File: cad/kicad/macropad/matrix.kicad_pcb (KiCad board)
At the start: 2 copper layers, 185.5 x 88.9 mm, 54 parts, among them J1 Conn_01x27, J2 Conn_01x27, J3 Conn_01x18, U1 74HC154, U2 MCP4821, U5 CMP04, U6 CMP04

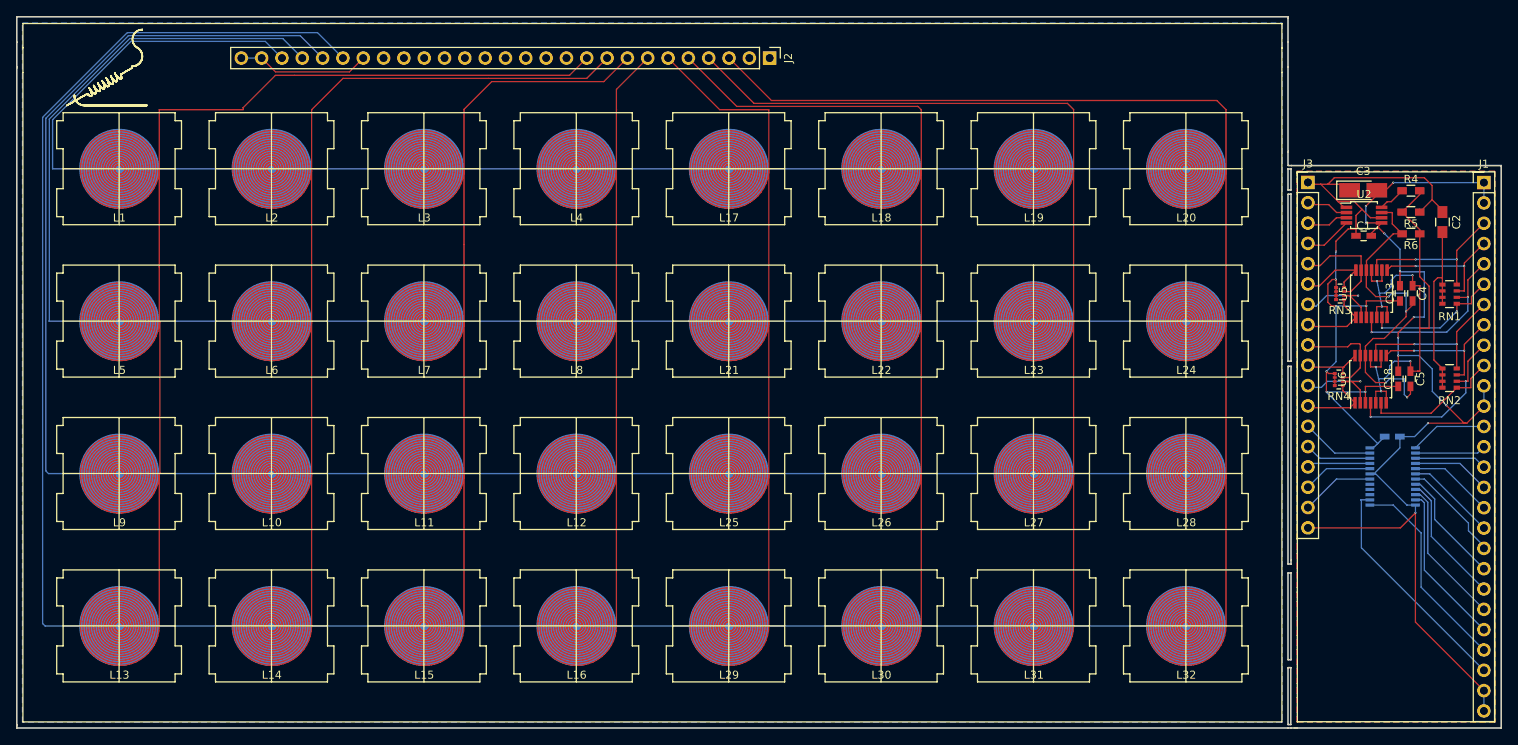
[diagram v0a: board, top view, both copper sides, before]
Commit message: seperated the controller from the demo macropad, remade the controller to hopefully be less succeptable to emi, and digital interferance.
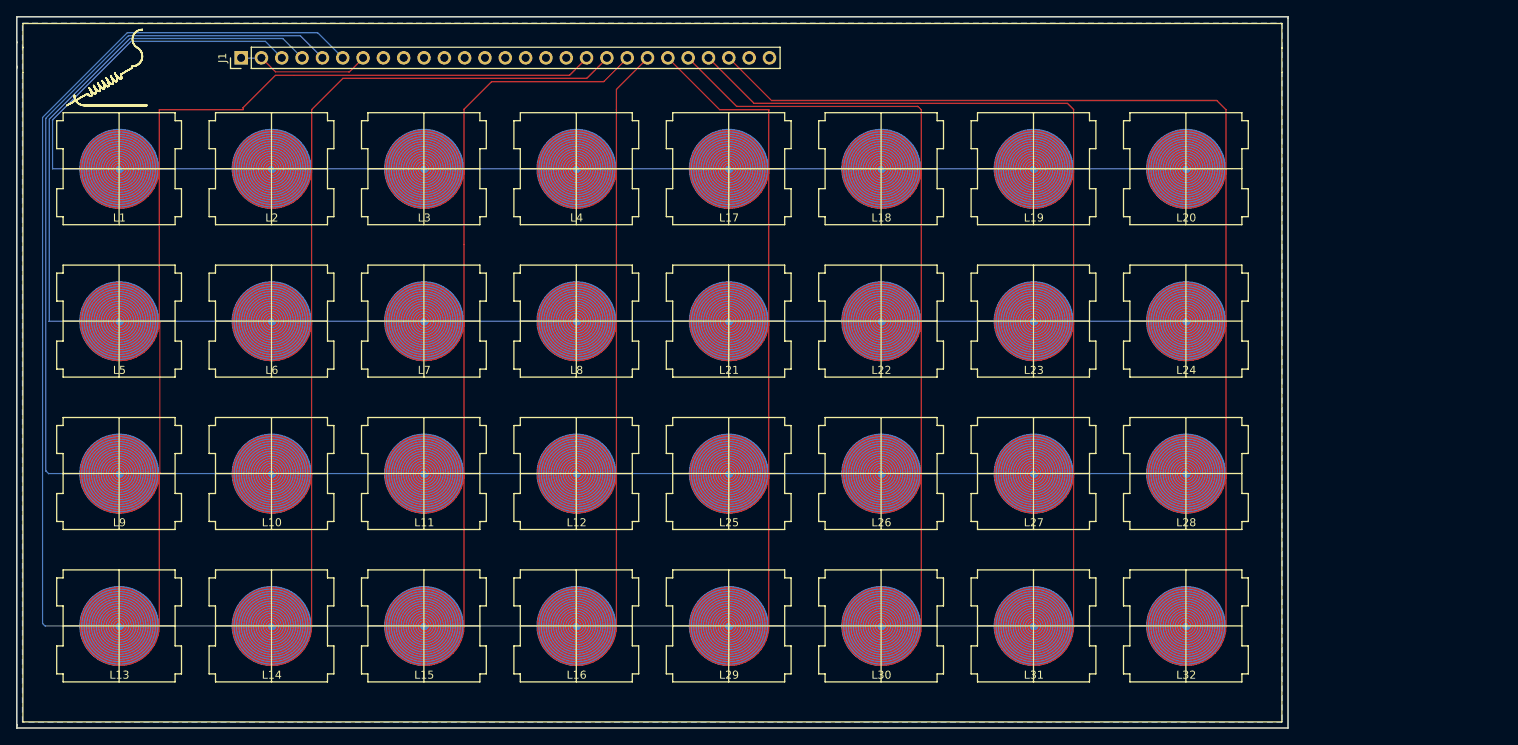
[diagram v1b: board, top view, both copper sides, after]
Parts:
- removed C1, C13, C18: 0u1, Capacitors_SMD:C_0603_HandSoldering
- removed C2: 100u, Capacitors_SMD:C_0805_HandSoldering
- removed C3: 10u-T, Capacitors_Tantalum_SMD:CP_Tantalum_Case-R_EIA-2012-12_Hand
- removed C4, C5, C9: 1u, Capacitors_SMD:C_0603_HandSoldering
- removed J2: Conn_01x27, Pin_Headers:Pin_Header_Straight_1x27_Pitch2.54mm
- removed J3: Conn_01x18, Pin_Headers:Pin_Header_Straight_1x18_Pitch2.54mm
- removed R4, R5: 20k, Resistors_SMD:R_0603_HandSoldering
- removed R6: 4k7, Resistors_SMD:R_0603_HandSoldering
- removed RN1, RN2: 330, Resistors_SMD:R_Array_Convex_4x0603
- removed RN3, RN4: 66k, Resistors_SMD:R_Array_Convex_4x0402
- removed U1: 74HC154, Housings_SSOP:TSSOP-24_4.4x7.8mm_Pitch0.65mm
- removed U2: MCP4821, Housings_SSOP:MSOP-8_3x3mm_Pitch0.65mm
- removed U5, U6: CMP04, Housings_SSOP:TSSOP-14_4.4x5mm_Pitch0.65mm
- moved J1 156.1 mm to (78.2, 48.3), turned to 90 degrees
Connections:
- J1 pad 1: GND -> GNDREF
- J1 pad 10: M8 -> GNDREF
- J1 pad 11: GND -> GNDREF
- J1 pad 12: GND -> GNDREF
- J1 pad 13: CS1 -> GNDREF
- J1 pad 14: CS2 -> GNDREF
- J1 pad 15: CS3 -> GNDREF
- J1 pad 16: CS4 -> GNDREF
- J1 pad 17: CS5 -> GNDREF
- J1 pad 18: CS6 -> /MRP1
- J1 pad 19: CS7 -> /MRP2
- J1 pad 2: GND -> GNDREF
- J1 pad 20: CS8 -> /MRP3
- J1 pad 21: CS9 -> /MRP4
- J1 pad 22: CS10 -> /MRP5
- J1 pad 23: CS11 -> /MRP6
- J1 pad 24: CS12 -> /MRP7
- J1 pad 25: CS13 -> /MRP8
- J1 pad 26: GND -> GNDREF
- J1 pad 27: GND -> GNDREF
- J1 pad 3: M1 -> /MCN13
- J1 pad 4: M2 -> /MCN12
- J1 pad 5: M3 -> /MCN11
- J1 pad 6: M4 -> /MCN10
- J1 pad 7: M5 -> GNDREF
- J1 pad 8: M6 -> GNDREF
- J1 pad 9: M7 -> GNDREF
- L1 pad 1: /matrix/MRP1 -> /MRP1
- L1 pad 2: /matrix/MCN13 -> /MCN13
- L10 pad 1: /matrix/MRP2 -> /MRP2
- L10 pad 2: /matrix/MCN11 -> /MCN11
- L11 pad 1: /matrix/MRP3 -> /MRP3
- L11 pad 2: /matrix/MCN11 -> /MCN11
- L12 pad 1: /matrix/MRP4 -> /MRP4
- L12 pad 2: /matrix/MCN11 -> /MCN11
- L13 pad 1: /matrix/MRP1 -> /MRP1
- L13 pad 2: /matrix/MCN10 -> /MCN10
- L14 pad 1: /matrix/MRP2 -> /MRP2
- L14 pad 2: /matrix/MCN10 -> /MCN10
- L15 pad 1: /matrix/MRP3 -> /MRP3
- L15 pad 2: /matrix/MCN10 -> /MCN10
- L16 pad 1: /matrix/MRP4 -> /MRP4
- L16 pad 2: /matrix/MCN10 -> /MCN10
- L17 pad 1: /matrix/MRP5 -> /MRP5
- L17 pad 2: /matrix/MCN13 -> /MCN13
- L18 pad 1: /matrix/MRP6 -> /MRP6
- L18 pad 2: /matrix/MCN13 -> /MCN13
- L19 pad 1: /matrix/MRP7 -> /MRP7
- L19 pad 2: /matrix/MCN13 -> /MCN13
- L2 pad 1: /matrix/MRP2 -> /MRP2
- L2 pad 2: /matrix/MCN13 -> /MCN13
- L20 pad 1: /matrix/MRP8 -> /MRP8
- L20 pad 2: /matrix/MCN13 -> /MCN13
- L21 pad 1: /matrix/MRP5 -> /MRP5
- L21 pad 2: /matrix/MCN12 -> /MCN12
- L22 pad 1: /matrix/MRP6 -> /MRP6
- L22 pad 2: /matrix/MCN12 -> /MCN12
- L23 pad 1: /matrix/MRP7 -> /MRP7
- L23 pad 2: /matrix/MCN12 -> /MCN12
- L24 pad 1: /matrix/MRP8 -> /MRP8
- L24 pad 2: /matrix/MCN12 -> /MCN12
- L25 pad 1: /matrix/MRP5 -> /MRP5
- L25 pad 2: /matrix/MCN11 -> /MCN11
- L26 pad 1: /matrix/MRP6 -> /MRP6
- L26 pad 2: /matrix/MCN11 -> /MCN11
- L27 pad 1: /matrix/MRP7 -> /MRP7
- L27 pad 2: /matrix/MCN11 -> /MCN11
- L28 pad 1: /matrix/MRP8 -> /MRP8
- L28 pad 2: /matrix/MCN11 -> /MCN11
- L29 pad 1: /matrix/MRP5 -> /MRP5
- L29 pad 2: /matrix/MCN10 -> /MCN10
- L3 pad 1: /matrix/MRP3 -> /MRP3
- L3 pad 2: /matrix/MCN13 -> /MCN13
- L30 pad 1: /matrix/MRP6 -> /MRP6
- L30 pad 2: /matrix/MCN10 -> /MCN10
- L31 pad 1: /matrix/MRP7 -> /MRP7
- L31 pad 2: /matrix/MCN10 -> /MCN10
- L32 pad 1: /matrix/MRP8 -> /MRP8
- L32 pad 2: /matrix/MCN10 -> /MCN10
- L4 pad 1: /matrix/MRP4 -> /MRP4
- L4 pad 2: /matrix/MCN13 -> /MCN13
- L5 pad 1: /matrix/MRP1 -> /MRP1
- L5 pad 2: /matrix/MCN12 -> /MCN12
- L6 pad 1: /matrix/MRP2 -> /MRP2
- L6 pad 2: /matrix/MCN12 -> /MCN12
- L7 pad 1: /matrix/MRP3 -> /MRP3
- L7 pad 2: /matrix/MCN12 -> /MCN12
- L8 pad 1: /matrix/MRP4 -> /MRP4
- L8 pad 2: /matrix/MCN12 -> /MCN12
- L9 pad 1: /matrix/MRP1 -> /MRP1
- L9 pad 2: /matrix/MCN11 -> /MCN11
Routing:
- net /matrix/MCN10: track 249.7 -> 0.00 mm
- net /MCN10: track 0.00 -> 249.7 mm
- net /matrix/MCN11: track 229.4 -> 0.00 mm
- net /MCN11: track 0.00 -> 229.4 mm
- net /matrix/MCN12: track 208.8 -> 0.00 mm
- net /MCN12: track 0.00 -> 208.8 mm
- net /matrix/MCN13: track 181.4 -> 0.00 mm
- net /MCN13: track 0.00 -> 181.4 mm
- net GND: track 181.1 -> 0.00 mm, vias 15 -> 0
- net /matrix/MRP8: track 129.3 -> 0.00 mm
- net /MRP8: track 0.00 -> 129.3 mm
- net /matrix/MRP1: track 120.9 -> 0.00 mm
- net /MRP1: track 0.00 -> 120.9 mm
- net /matrix/MRP7: track 112.9 -> 0.00 mm
- net /MRP7: track 0.00 -> 112.9 mm
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- removed copper zone on B.Cu, net GND
- removed copper zone on F.Cu, net GND
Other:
- board size 185.5 x 88.9 mm -> 158.9 x 88.9 mm
